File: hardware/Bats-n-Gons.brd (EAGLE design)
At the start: 59.4 x 53.3 mm, 54 parts, among them SW1 SMD_SWITCH, U1 SAMD51PXXA, U2 IS31AP4991, X4 32.768

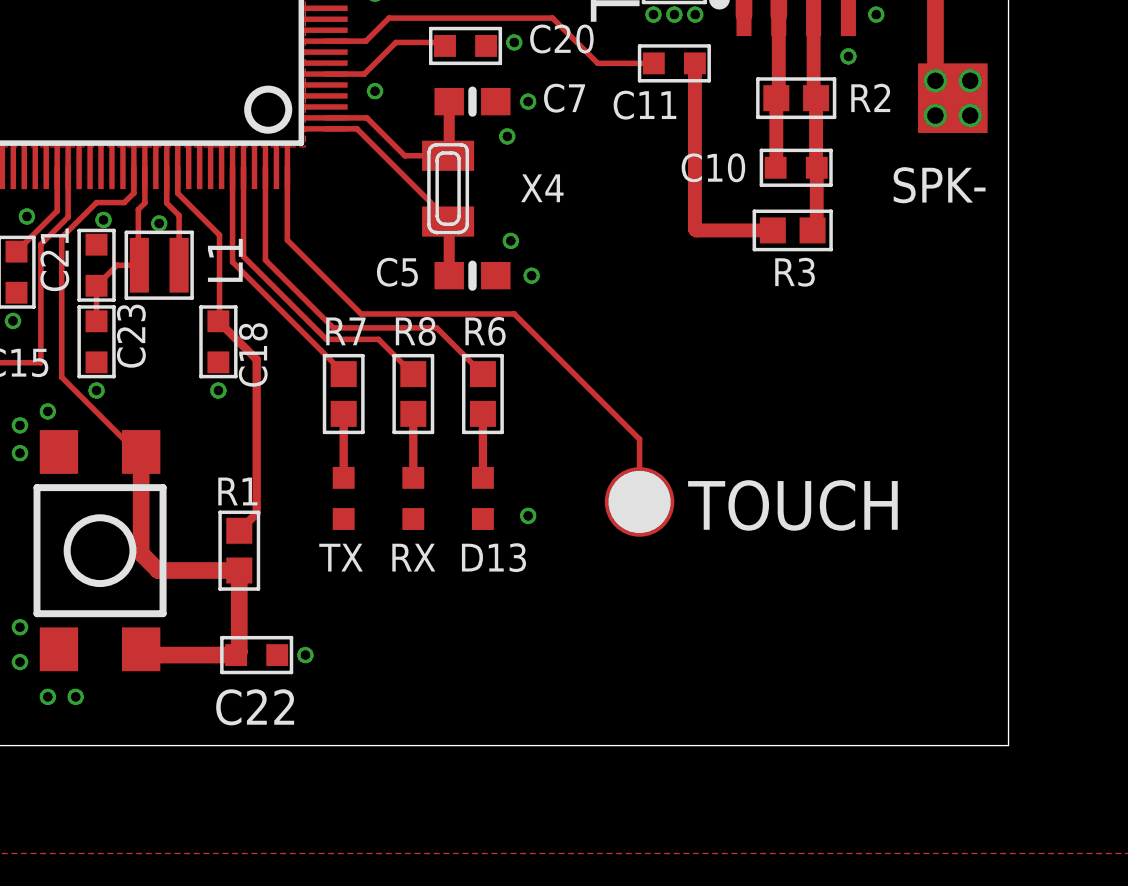
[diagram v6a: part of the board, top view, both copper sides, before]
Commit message: added SWD interface so we can actually install the bootloader :-)
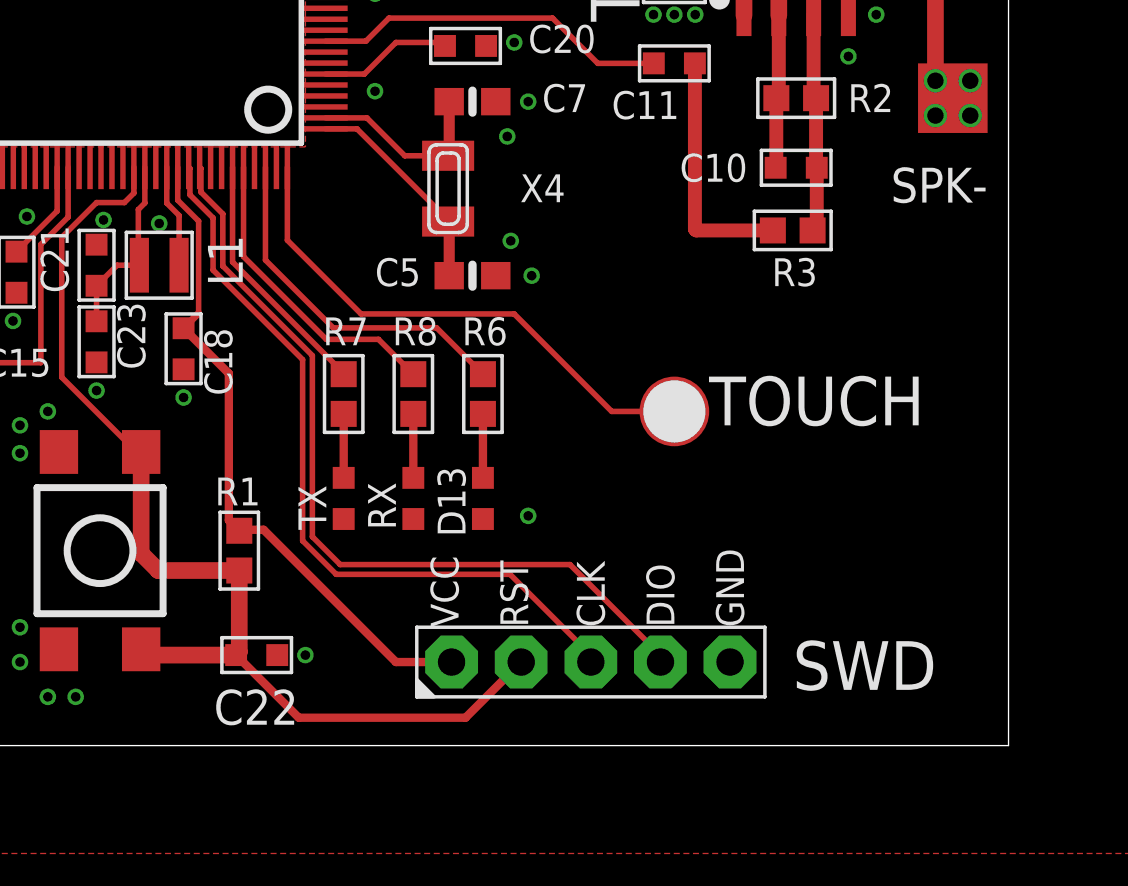
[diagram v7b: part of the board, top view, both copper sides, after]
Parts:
- added J2: (no value), bats-n-gons:HEADER_5PIN
- moved PAD_TOUCH 3.54 mm to (47.2, 12.2)
- moved C18 1.30 mm to (29.3, 14.5)
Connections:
- net !RESET!: now also J2.2
- net +3.3V: now also J2.1
- net GND: now also J2.5
- net SWCLK: now also J2.3
- net SWDIO: now also J2.4
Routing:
- net SWDIO: track 0.00 -> 29.9 mm
- net SWCLK: track 0.00 -> 27.8 mm
- net !RESET!: track 27.6 -> 39.8 mm
- net +3.3V: track 135.5 -> 145.2 mm
- net A2: track 20.8 -> 19.4 mm
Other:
- board text added: "CLK"
- board text added: "DIO"
- board text added: "RST"
- board text added: "SWD"
- board text added: "VCC"
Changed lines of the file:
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@@
 <drawing>
 <settings>
-<setting alwaysvectorfont="yes"/>
+<setting alwaysvectorfont="no"/>
 <setting verticaltext="up"/>
 </settings>
@@
 <text x="31.623" y="50.038" size="1.016" layer="21" ratio="12">TX</text>
 <text x="34.798" y="50.038" size="1.016" layer="21" ratio="12">GND</text>
-<text x="34.29" y="6.35" size="1.016" layer="25">TX</text>
-<text x="36.83" y="6.35" size="1.016" layer="25">RX</text>
+<text x="34.544" y="7.874" size="1.016" layer="25" rot="R90">TX</text>
+<text x="37.084" y="7.874" size="1.016" layer="25" rot="R90">RX</text>
 <polygon width="0.1524" layer="41">
 <vertex x="33.782" y="23.368"/>
@@
 <text x="42.672" y="46.99" size="1.778" layer="21">3/7/2020</text>
 <text x="41.148" y="44.196" size="1.778" layer="21">Kravitz/Yapo</text>
-<text x="47.752" y="7.874" size="1.778" layer="21">TOUCH</text>
-<text x="39.37" y="6.35" size="1.016" layer="25">D13</text>
+<text x="48.514" y="11.684" size="1.778" layer="21">TOUCH</text>
+<text x="39.624" y="7.62" size="1.016" layer="25" rot="R90">D13</text>
 <text x="4.572" y="42.672" size="1.4224" layer="21">+5</text>
 <text x="17.272" y="42.672" size="1.4224" layer="21">+3.3</text>
@@
 <text x="45.974" y="26.416" size="1.778" layer="21" rot="R90">TOUCH</text>
 <circle x="42.418" y="30.226" radius="1.077628125" width="0" layer="21"/>
-<circle x="45.974" y="8.89" radius="1.135921875" width="0" layer="21"/>
+<circle x="47.244" y="12.192" radius="1.135921875" width="0" layer="21"/>
+<text x="51.562" y="2.032" size="1.778" layer="21">SWD</text>
+<text x="39.37" y="4.318" size="1.016" layer="21" rot="R90">VCC</text>
+<text x="41.91" y="4.318" size="1.016" layer="21" rot="R90">RST</text>
+<text x="44.704" y="4.318" size="1.016" layer="21" rot="R90">CLK</text>
+<text x="47.244" y="4.318" size="1.016" layer="21" rot="R90">DIO</text>
+<text x="49.784" y="4.318" size="1.016" layer="21" rot="R90">GND</text>
 </plain>
 <attributes>
@@
 <attribute name="VALUE" x="23.495" y="37.338" size="1.27" layer="27" rot="R270"/>
 </element>
-<element name="C18" library="bats-n-gons" package="C0603" value="" x="30.607" y="14.732" smashed="yes" rot="R90">
-<attribute name="NAME" x="31.369" y="15.494" size="1.016" layer="25" rot="R270"/>
-<attribute name="VALUE" x="31.877" y="18.542" size="1.27" layer="27" rot="R90"/>
+<element name="C18" library="bats-n-gons" package="C0603" value="" x="29.337" y="14.478" smashed="yes" rot="R90">
+<attribute name="NAME" x="30.099" y="15.24" size="1.016" layer="25" rot="R270"/>
+<attribute name="VALUE" x="30.607" y="18.288" size="1.27" layer="27" rot="R90"/>
 </element>
 <element name="C19" library="bats-n-gons" package="C0603" value="" x="39.624" y="34.925" smashed="yes" rot="R180">
@@
 <attribute name="VALUE" x="11.176" y="2.9845" size="0.6096" layer="27" font="vector" ratio="20" align="top-center"/>
 </element>
-<element name="PAD_TOUCH" library="bats-n-gons" package="PAD-ROUND-100MIL-MASK" value="PAD" x="45.974" y="8.89" smashed="yes"/>
+<element name="PAD_TOUCH" library="bats-n-gons" package="PAD-ROUND-100MIL-MASK" value="PAD" x="47.244" y="12.192" smashed="yes"/>
 <element name="U$33" library="bats-n-gons" package="PAD-ROUND-50MIL" value="PADROUND-50MIL" x="18.542" y="41.91" smashed="yes"/>
 <element name="U$34" library="bats-n-gons" package="PAD-ROUND-50MIL" value="PADROUND-50MIL" x="3.556" y="43.18" smashed="yes"/>
@@
 </element>
 <element name="PAD_TOUCH1" library="bats-n-gons" package="PAD-ROUND-100MIL-MASK" value="PAD" x="42.418" y="30.226" smashed="yes"/>
+<element name="J2" library="bats-n-gons" package="HEADER_5PIN" value="" x="44.196" y="3.048" smashed="yes">
+<attribute name="VALUE" x="37.846" y="4.953" size="1.27" layer="27" font="vector"/>
+</element>
 </elements>
 <signals>
@@
 <via x="23.114" y="15.494" extent="1-16" drill="0.35"/>
 <wire x1="23.241" y1="16.522" x2="23.368" y2="16.395" width="0.1524" layer="1"/>
-<wire x1="30.607" y1="13.982" x2="30.734" y2="13.855" width="0.1524" layer="1"/>
+<wire x1="29.337" y1="13.728" x2="29.464" y2="13.601" width="0.1524" layer="1"/>
 <via x="26.162" y="12.954" extent="1-16" drill="0.35"/>
 <wire x1="23.229" y1="16.51" x2="23.241" y2="16.522" width="0.1524" layer="1"/>
@@
 <contactref element="C23" pad="P$1"/>
 <contactref element="C21" pad="P$1"/>
-<via x="30.607" y="12.954" extent="1-16" drill="0.35"/>
+<via x="29.337" y="12.7" extent="1-16" drill="0.35"/>
 <via x="26.416" y="19.177" extent="1-16" drill="0.35"/>
 <via x="36.322" y="31.75" extent="1-16" drill="0.35"/>
@@
 <via x="46.482" y="26.67" extent="1-16" drill="0.35"/>
 <via x="48.006" y="26.67" extent="1-16" drill="0.35"/>
+<contactref element="J2" pad="5"/>
 </signal>
 <signal name="AREF" class="4">
@@
 <contactref element="PAD_TOUCH" pad="P$1"/>
 <wire x1="33.124" y1="21.102" x2="33.124" y2="18.438" width="0.2032" layer="1"/>
-<wire x1="45.974" y1="11.176" x2="41.402" y2="15.748" width="0.2032" layer="1"/>
-<wire x1="45.974" y1="11.176" x2="45.974" y2="8.89" width="0.2032" layer="1"/>
+<wire x1="44.958" y1="12.192" x2="41.402" y2="15.748" width="0.2032" layer="1"/>
+<wire x1="44.958" y1="12.192" x2="47.244" y2="12.192" width="0.2032" layer="1"/>
 <wire x1="33.124" y1="18.438" x2="35.814" y2="15.748" width="0.2032" layer="1"/>
 <wire x1="35.814" y1="15.748" x2="41.402" y2="15.748" width="0.2032" layer="1"/>
@@
 <signal name="SWCLK">
 <contactref element="U1" pad="119"/>
+<contactref element="J2" pad="3"/>
+<wire x1="29.524" y1="21.102" x2="29.5684" y2="21.0576" width="0.2032" layer="1"/>
+<wire x1="30.4128" y1="19.2510875" x2="30.4128" y2="17.3494" width="0.2032" layer="1"/>
+<wire x1="33.6804" y1="14.0818" x2="33.6804" y2="7.4727" width="0.2032" layer="1"/>
+<wire x1="30.4128" y1="17.3494" x2="33.6804" y2="14.0818" width="0.2032" layer="1"/>
+<wire x1="33.6804" y1="7.4727" x2="34.9047" y2="6.2484" width="0.2032" layer="1"/>
+<wire x1="34.9047" y1="6.2484" x2="41.2496" y2="6.2484" width="0.2032" layer="1"/>
+<wire x1="29.5684" y1="21.0576" x2="29.5684" y2="20.0954875" width="0.2032" layer="1"/>
+<wire x1="29.5684" y1="20.0954875" x2="30.4128" y2="19.2510875" width="0.2032" layer="1"/>
+<wire x1="44.196" y1="3.302" x2="44.196" y2="3.048" width="0.2032" layer="1"/>
+<wire x1="41.2496" y1="6.2484" x2="44.196" y2="3.302" width="0.2032" layer="1"/>
 </signal>
 <signal name="SWDIO">
 <contactref element="U1" pad="120"/>
+<contactref element="J2" pad="4"/>
+<wire x1="29.924" y1="21.102" x2="29.97" y2="21.056" width="0.2032" layer="1"/>
+<wire x1="29.97" y1="21.056" x2="29.97" y2="20.1967875" width="0.2032" layer="1"/>
+<wire x1="34.036" y1="14.2291" x2="34.036" y2="7.62" width="0.2032" layer="1"/>
+<wire x1="30.7684" y1="17.4967" x2="34.036" y2="14.2291" width="0.2032" layer="1"/>
+<wire x1="30.7684" y1="19.3983875" x2="30.7684" y2="17.4967" width="0.2032" layer="1"/>
+<wire x1="29.97" y1="20.1967875" x2="30.7684" y2="19.3983875" width="0.2032" layer="1"/>
+<wire x1="34.036" y1="7.62" x2="35.052" y2="6.604" width="0.2032" layer="1"/>
+<wire x1="35.052" y1="6.604" x2="43.434" y2="6.604" width="0.2032" layer="1"/>
+<wire x1="43.434" y1="6.604" x2="46.736" y2="3.302" width="0.2032" layer="1"/>
+<wire x1="46.736" y1="3.302" x2="46.736" y2="3.048" width="0.2032" layer="1"/>
 </signal>
 <signal name="USB_HOSTEN">
@@
 <contactref element="R5" pad="P$1"/>
 <wire x1="38.331" y1="28.102" x2="38.874" y2="28.067" width="0.254" layer="1"/>
-<wire x1="30.648" y1="15.523" x2="30.607" y2="15.482" width="0.254" layer="1"/>
+<wire x1="29.886" y1="15.777" x2="29.337" y2="15.228" width="0.254" layer="1"/>
 <wire x1="34.524" y1="32.502" x2="38.872" y2="32.502" width="0.2032" layer="1"/>
 <wire x1="38.872" y1="32.502" x2="38.989" y2="32.385" width="0.2032" layer="1"/>
@@
 <wire x1="18.542" y1="41.91" x2="18.542" y2="45.212" width="0.6096" layer="1"/>
 <wire x1="18.542" y1="45.212" x2="18.288" y2="45.466" width="0.6096" layer="1"/>
-<wire x1="29.124" y1="21.102" x2="29.124" y2="20.152" width="0.2032" layer="1"/>
-<wire x1="30.648" y1="18.628" x2="30.648" y2="15.523" width="0.2032" layer="1"/>
-<wire x1="29.124" y1="20.152" x2="30.648" y2="18.628" width="0.2032" layer="1"/>
-<wire x1="30.607" y1="15.482" x2="32.004" y2="14.085" width="0.3048" layer="1"/>
-<wire x1="32.004" y1="8.472" x2="31.369" y2="7.837" width="0.3048" layer="1"/>
-<wire x1="32.004" y1="14.085" x2="32.004" y2="8.472" width="0.3048" layer="1"/>
+<wire x1="29.124" y1="21.102" x2="29.124" y2="19.898" width="0.2032" layer="1"/>
+<wire x1="29.886" y1="19.136" x2="29.886" y2="15.777" width="0.2032" layer="1"/>
+<wire x1="29.124" y1="19.898" x2="29.886" y2="19.136" width="0.2032" layer="1"/>
+<wire x1="29.337" y1="15.228" x2="30.988" y2="13.577" width="0.3048" layer="1"/>
+<wire x1="31.369" y1="7.837" x2="30.988" y2="8.218" width="0.3048" layer="1"/>
+<wire x1="30.988" y1="13.577" x2="30.988" y2="8.218" width="0.3048" layer="1"/>
 <contactref element="C24" pad="P$2"/>
 <wire x1="31.524" y1="36.302" x2="31.524" y2="38.128" width="0.2032" layer="1"/>
 <wire x1="31.524" y1="38.128" x2="32.004" y2="38.608" width="0.2032" layer="1"/>
 <wire x1="32.004" y1="38.608" x2="32.004" y2="39.382" width="0.2032" layer="1"/>
+<contactref element="J2" pad="1"/>
+<wire x1="39.116" y1="3.048" x2="37.084" y2="3.048" width="0.3048" layer="1"/>
+<wire x1="37.084" y1="3.048" x2="32.258" y2="7.874" width="0.3048" layer="1"/>
+<wire x1="32.258" y1="7.874" x2="31.406" y2="7.874" width="0.3048" layer="1"/>
+<wire x1="31.406" y1="7.874" x2="31.369" y2="7.837" width="0.3048" layer="1"/>
 </signal>
 <signal name="+5V">
@@
 <wire x1="27.35269375" y1="10.977" x2="27.524" y2="10.977" width="0.2032" layer="1"/>
 <wire x1="24.892" y1="18.542" x2="24.892" y2="13.43769375" width="0.2032" layer="1"/>
+<contactref element="J2" pad="2"/>
+<wire x1="41.656" y1="3.048" x2="39.624" y2="1.016" width="0.3048" layer="1"/>
+<wire x1="33.54" y1="1.016" x2="31.254" y2="3.302" width="0.3048" layer="1"/>
+<wire x1="39.624" y1="1.016" x2="33.54" y2="1.016" width="0.3048" layer="1"/>
 </signal>
 <signal name="N$8">
